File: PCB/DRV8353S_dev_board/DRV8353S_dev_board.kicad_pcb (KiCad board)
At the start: 4 copper layers, 100 x 100 mm, 139 parts, among them J1 HC_POWER, J2 MOT_LC, J3 SWD, J4 EXT_CMD, J5 PHASE, Q1 BSS84, Q2 CSD19502, Q3 CSD19502, Q4 CSD19502, Q5 CSD19502, Q6 CSD19502, Q7 CSD19502, SW1 B3U, SW2 B3U, SW3 B3U, SW4 B3U, SW5 DIP, U1 ECS-33B, U2 STM32F042K4Ux, U3 MIC5283-3.3ML-TR, U4 MIC5283-5.0ML-TR, U5 DRV8353SM

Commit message: more routing work
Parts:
- added C35: 22nF, Capacitor_SMD:C_0603_1608Metric, F.Cu at (86.0, 125.4)
- added R56: 330, Resistor_SMD:R_0603_1608Metric, F.Cu at (86.0, 123.9)
- added REF**: MountingHole_3mm_Pad_Via, MountingHole:MountingHole_3mm_Pad_Via, F.Cu at (145.0, 130.0)
- added REF**: MountingHole_3mm_Pad_Via, MountingHole:MountingHole_3mm_Pad_Via, F.Cu at (55.0, 130.0)
- added TP20: THT, DRV8353S_dev_board:keystone_5001, F.Cu at (62.8, 105.5)
- C14, C15, C16: moved to B.Cu
- moved TP2 211.1 mm to (65.0, 86.1)
- moved TP1 211.0 mm to (64.6, 95.1)
- moved D4 205.6 mm to (56.1, 111.6), turned to 180 degrees
- moved C4 204.9 mm to (57.5, 99.4), turned to 90 degrees
- moved D5 196.8 mm to (61.5, 123.2), turned to 180 degrees
- moved C19 193.4 mm to (79.4, 156.4)
- moved R26 191.3 mm to (79.2, 159.0)
- moved D3 189.0 mm to (63.6, 131.6), turned to 90 degrees
- moved C1 188.4 mm to (77.5, 125.0), turned to 90 degrees
- moved C3 188.3 mm to (58.0, 85.2), turned to 270 degrees
- moved C17 187.9 mm to (86.0, 122.4)
- moved D6 187.4 mm to (65.2, 131.7), turned to 90 degrees
- moved R7 185.4 mm to (61.9, 128.6), turned to 90 degrees
- moved C15 185.2 mm to (72.1, 117.8), turned to 90 degrees
- moved C13 183.3 mm to (65.0, 89.6), turned to 270 degrees
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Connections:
- R10 pad 1: /HALLB_JMP -> /HALLB
- R21 pad 1: /HALLC_JMP -> /HALLC
- R9 pad 1: /HALLA_JMP -> /HALLA
- TP3 pad 1: /HALLA_JMP -> /HALLA
- TP5 pad 1: /HALLB_JMP -> /HALLB
- TP6 pad 1: /HALLC_JMP -> /HALLC
- U2 pad 6: /I_PHASE_A_JMP -> /MOT_TEMP_JMP
- U2 pad 7: /I_PHASE_B_JMP -> /I_PHASE_C_JMP
- U2 pad 8: /I_PHASE_C_JMP -> /I_PHASE_B_JMP
- U2 pad 9: /MOT_TEMP -> /I_PHASE_A_JMP
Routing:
- net GND: track 126.7 -> 2.00 mm, vias 57 -> 1
- net /GATE_HI_C: track 80.7 -> 0.00 mm, vias 2 -> 0
- net /HALLC: track 0.00 -> 79.7 mm, vias 0 -> 1
- net /HALLA: track 0.00 -> 73.4 mm, vias 0 -> 2
- net /HALLB: track 0.00 -> 71.4 mm, vias 0 -> 2
- net /GATE_LO_C: track 61.2 -> 0.00 mm, vias 2 -> 0
- net /DIRECTION_DIP: track 0.00 -> 60.6 mm
- net /MOT_C: track 57.2 -> 0.00 mm, vias 21 -> 0
- net /SHUNT_POS_C: track 56.0 -> 0.00 mm, vias 2 -> 0
- net /~SPEED_UP_PB: track 0.00 -> 52.2 mm
- net /~SPEED_DOWN_PB: track 0.00 -> 47.5 mm
- net /GATE_HI_B: track 43.7 -> 0.00 mm, vias 2 -> 0
- net /~BRAKE_PB: track 0.00 -> 41.1 mm
- net /~RESET_PB: track 0.00 -> 36.2 mm, vias 0 -> 2
- net /GATE_LO_B: track 33.7 -> 0.00 mm, vias 2 -> 0
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- removed copper zone on B.Cu, net (none)
- removed copper zone on B.Cu, net /MOT_A
- removed copper zone on F.Cu, net /MOT_A
- removed copper zone on In1.Cu, net /MOT_A
- removed copper zone on B.Cu, net /MOT_B
- removed copper zone on F.Cu, net /MOT_B
- removed copper zone on In1.Cu, net /MOT_B
- removed copper zone on B.Cu, net /MOT_C
- removed copper zone on F.Cu, net /MOT_C
- removed copper zone on In1.Cu, net /MOT_C
- removed copper zone on F.Cu, net /SHUNT_POS_A
- removed copper zone on F.Cu, net /SHUNT_POS_B
- removed copper zone on F.Cu, net /SHUNT_POS_C
- removed copper zone on B.Cu, net GND
- removed copper zone on F.Cu, net GND
- removed copper zone on In1.Cu, net GND
- removed copper zone on In2.Cu, net GND
- removed copper zone on F.Cu, net Vdrive
- removed copper zone on In1.Cu, net Vdrive
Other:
- board size 100 x 100 mm -> 100 x 85 mm

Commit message: Final (?) layout
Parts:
- removed R36, R37: 0, Resistor_SMD:R_0603_1608Metric
- moved R16 99.9 mm to (65.8, 115.6), turned to 180 degrees
- moved R33 96.1 mm to (78.9, 110.2), turned to 270 degrees
- moved R17 95.2 mm to (65.8, 117.2), turned to 180 degrees
- moved R18 86.2 mm to (71.1, 110.2), turned to 90 degrees
- moved C31 83.3 mm to (95.4, 105.4), turned to 180 degrees
- moved R15 67.5 mm to (76.0, 125.0), turned to 270 degrees
- moved TP20 60.8 mm to (123.0, 97.0)
- moved C23 58.8 mm to (65.8, 112.6), turned to 180 degrees
- moved R32 56.0 mm to (65.8, 114.1)
- moved R34 50.6 mm to (74.5, 126.8), turned to 90 degrees
- moved R27 49.7 mm to (69.6, 110.2), turned to 90 degrees
- moved R26 49.0 mm to (74.3, 110.3), turned to 270 degrees
- moved C21 48.8 mm to (68.1, 110.2), turned to 90 degrees
- moved C22 46.9 mm to (65.8, 120.2)
- moved C19 46.6 mm to (72.7, 110.2), turned to 90 degrees
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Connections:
- J3 pad 2: Net-(D4-Pad2) -> GND
- J3 pad 4: /~RESET_PB -> Net-(J3-Pad4)
- J3 pad 5: Net-(J3-Pad5) -> Net-(D4-Pad2)
- J3 pad 6: GND -> /~RESET_PB
- TP20 pad 1: /MOT_TEMP_JMP -> /MOT_TEMP
- U2 pad 14: /SPEED_PWM_JMP -> /~DRV8353_FAULT_JMP
- U2 pad 15: /DIRECTION_JMP -> /DRV8353_EN_JMP
- U2 pad 16: /~BRAKE_JMP -> /DIRECTION_JMP
- U2 pad 18: /DRV8353_EN_JMP -> /~BRAKE_JMP
- U2 pad 21: /DIRECTION_DIP -> /~SYS_FAULT
- U2 pad 22: /~SPEED_UP_PB -> /~LED_SPEED
- U2 pad 25: Net-(U2-Pad25) -> /~LED_DIR
- U2 pad 26: /~DRV8353_FAULT_JMP -> /~BRAKE_PB
- U2 pad 27: /~LED_DIR -> /~SPEED_DOWN_PB
- U2 pad 28: /~LED_SPEED -> /~SPEED_UP_PB
- U2 pad 29: /~SYS_FAULT -> /DIRECTION_DIP
- U2 pad 30: /~SPEED_DOWN_PB -> Net-(U2-Pad30)
- U2 pad 32: /~BRAKE_PB -> /SPEED_PWM_JMP
- U2 pad 6: /MOT_TEMP_JMP -> /I_PHASE_C_JMP
- U2 pad 7: /I_PHASE_C_JMP -> /I_PHASE_B_JMP
- U2 pad 8: /I_PHASE_B_JMP -> /I_PHASE_A_JMP
- U2 pad 9: /I_PHASE_A_JMP -> /MOT_TEMP_JMP
- U5 pad 41: (no net) -> GND
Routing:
- net /HALLC: track 79.7 -> 0.00 mm, vias 1 -> 0
- net /HALLA: track 73.4 -> 0.00 mm, vias 2 -> 0
- net /HALLB: track 71.4 -> 0.00 mm, vias 2 -> 0
- net /DIRECTION_DIP: track 60.6 -> 0.00 mm
- net /~SPEED_UP_PB: track 52.2 -> 0.00 mm
- net /~SPEED_DOWN_PB: track 47.5 -> 0.00 mm
- net /~BRAKE_PB: track 41.1 -> 0.00 mm
- net /~RESET_PB: track 36.2 -> 0.00 mm, vias 2 -> 0
- net /~DRV8353_FAULT: track 19.7 -> 0.00 mm
- net /I_PHASE_C: track 19.3 -> 0.00 mm
- net /EXT_UART_RX: track 18.9 -> 0.00 mm, vias 2 -> 0
- net /I_PHASE_B: track 18.7 -> 0.00 mm
- net /I_PHASE_A: track 18.2 -> 0.00 mm
- net /EXT_UART_TX: track 17.8 -> 0.00 mm
- net /MOT_TEMP_JMP: track 14.3 -> 0.00 mm
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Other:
- outline, holes or cut-outs redrawn
- board text added: "High Current Stack up: Top: Vdrive Mid1: Vdrive Mid2: DRV Sig and GND Bottom: GND"
- board text added: "Low Current Stack up: Top: Signal Mid1: GND Mid2: Power Bottom: Signal + GND"

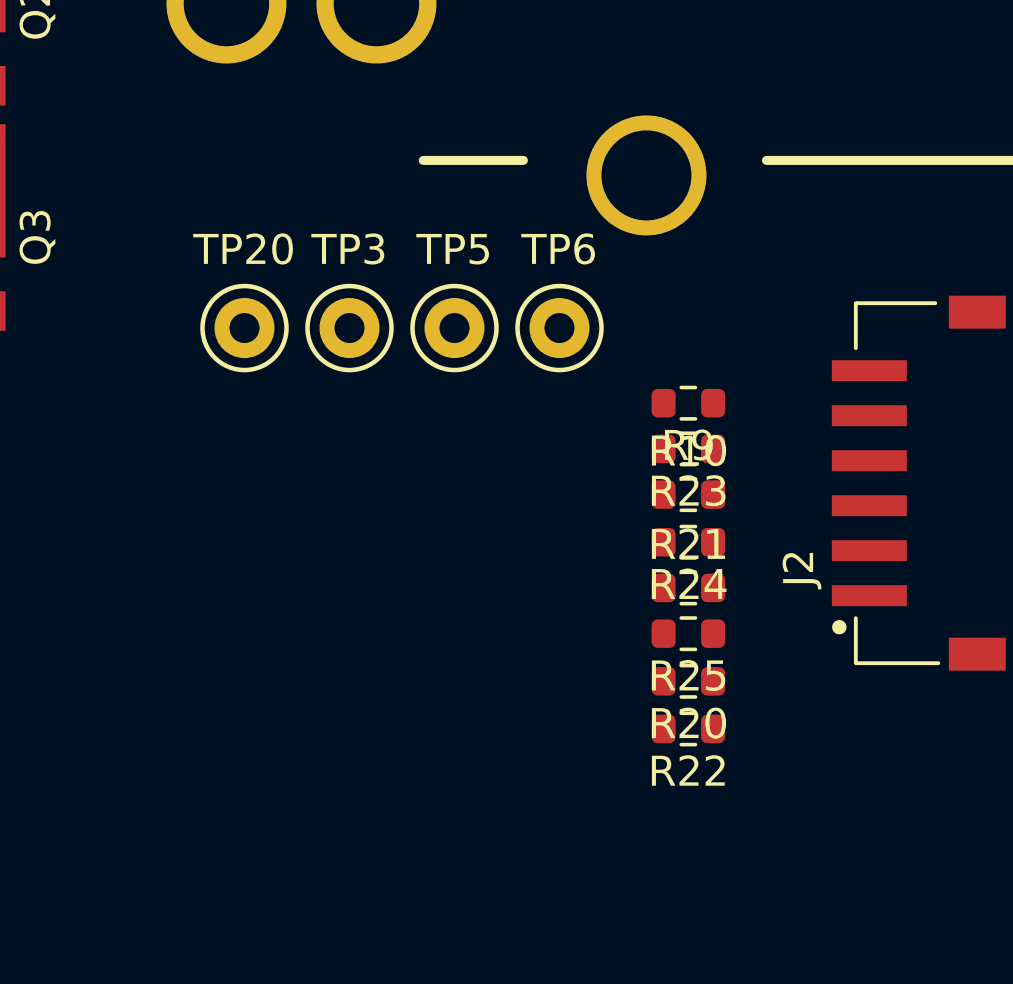
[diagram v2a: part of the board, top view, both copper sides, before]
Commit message: Final Routing
Moved around encoder stuff. Also added decoupling capacitor near encoder connector.
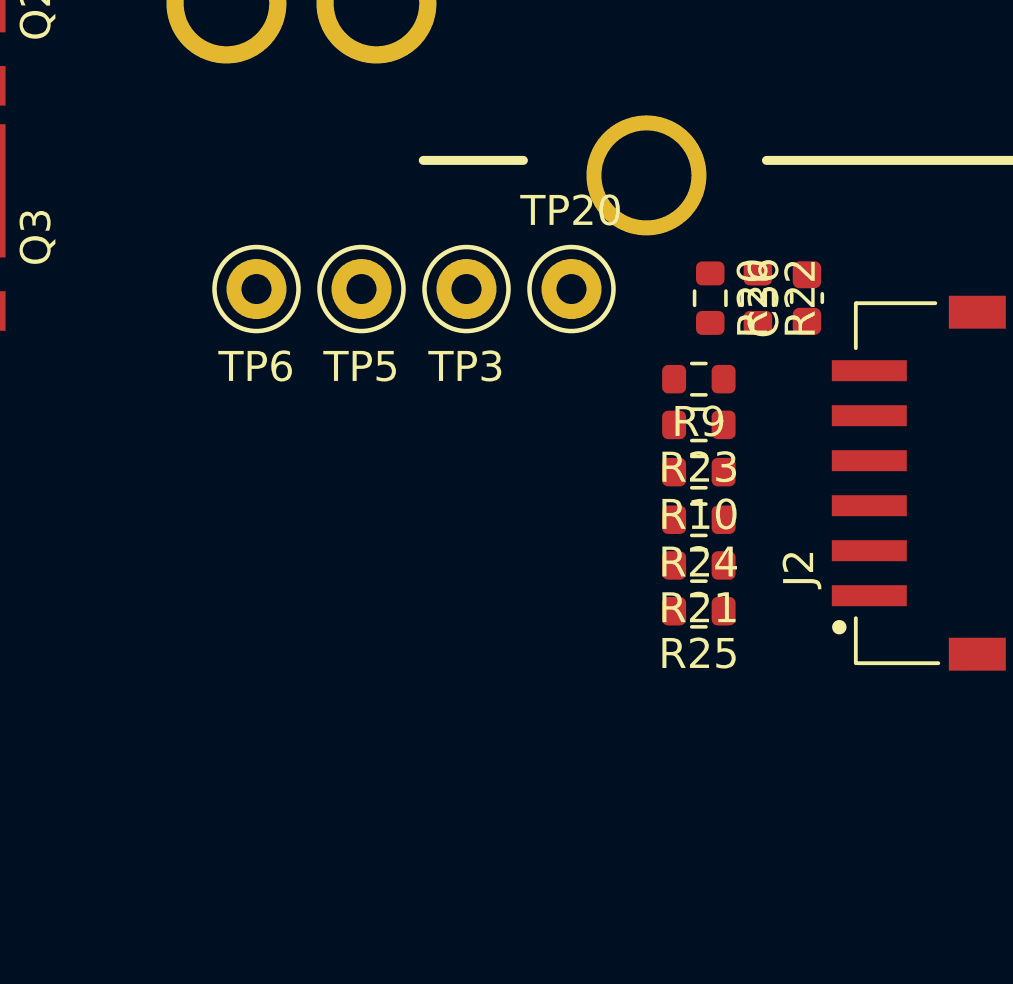
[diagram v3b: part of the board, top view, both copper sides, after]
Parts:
- added C36: 22nF, Capacitor_SMD:C_0603_1608Metric, F.Cu at (141.8, 96.0)
- moved R22 14.5 mm to (140.1, 96.0), turned to 270 degrees
- moved R20 12.8 mm to (138.5, 96.0), turned to 270 degrees
- moved TP20 11.0 mm to (133.9, 95.7)
- moved TP6 10.2 mm to (123.4, 95.7), turned to 180 degrees
- moved TP3 4.11 mm to (130.4, 95.7), turned to 180 degrees
- moved TP5 3.36 mm to (126.9, 95.7), turned to 180 degrees
- moved R9 0.87 mm to (138.1, 98.7)
- moved R23 0.87 mm to (138.1, 100.2)
- moved R10 0.83 mm to (138.1, 101.8), turned to 180 degrees
- moved R21 0.83 mm to (138.1, 104.9), turned to 180 degrees
- moved R25 0.83 mm to (138.1, 106.4)
- moved R24 0.83 mm to (138.1, 103.4)
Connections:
- R10 pad 1: /HALLB -> /HALLB_JMP
- R21 pad 1: /HALLC -> /HALLC_JMP
- R9 pad 1: /HALLA -> /HALLA_JMP

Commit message: High Current Routing
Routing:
- net Vdrive: vias 0 -> 91
- net GND: vias 0 -> 146
- net /MOT_C: vias 0 -> 48
- net /MOT_B: vias 0 -> 49
- net /MOT_A: vias 0 -> 50
- added copper zone on B.Cu, net /MOT_A
- added copper zone on F.Cu, net /MOT_A
- added copper zone on In1.Cu, net /MOT_A
- added copper zone on In2.Cu, net /MOT_A
- added copper zone on B.Cu, net /MOT_B
- added copper zone on F.Cu, net /MOT_B
- added copper zone on In1.Cu, net /MOT_B
- added copper zone on In2.Cu, net /MOT_B
- added copper zone on B.Cu, net /MOT_C
- added copper zone on F.Cu, net /MOT_C
- added copper zone on In1.Cu, net /MOT_C
- added copper zone on In2.Cu, net /MOT_C
- added copper zone on F.Cu, net /SHUNT_POS_A
- added copper zone on F.Cu, net /SHUNT_POS_B
- added copper zone on F.Cu, net /SHUNT_POS_C
- added copper zone on B.Cu, net GND
- added copper zone on F.Cu, net GND
- added copper zone on In1.Cu, net GND
- added copper zone on In2.Cu, net GND
- added copper zone on F.Cu, net Vdrive
- added copper zone on In1.Cu, net Vdrive

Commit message: Most DRV routing done.
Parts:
- moved TP10 6.99 mm to (67.5, 104.7)
- moved TP12 6.99 mm to (71.0, 104.7)
- moved TP8 6.99 mm to (74.5, 104.7)
- moved TP9 6.99 mm to (64.0, 104.7)
- moved C22 2.90 mm to (68.5, 121.3)
- moved C23 2.90 mm to (68.5, 113.7)
- moved R16 2.90 mm to (68.5, 116.8)
- moved R17 2.90 mm to (68.5, 118.3)
- moved R28 2.90 mm to (68.5, 119.8)
- moved R32 2.90 mm to (68.5, 115.3)
- moved C17 1.14 mm to (85.7, 124.7)
- moved C18 1.14 mm to (85.7, 121.6)
- moved C20 1.14 mm to (85.7, 118.5)
- moved C35 1.14 mm to (85.7, 115.4)
- moved R29 1.14 mm to (85.7, 117.0)
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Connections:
- REF** pad 1: (no net) -> GND (x4)
- TP11 pad 1: /I_PHASE_A_JMP -> /I_PHASE_A
- TP4 pad 1: /I_PHASE_C_JMP -> /I_PHASE_C
- TP7 pad 1: /I_PHASE_B_JMP -> /I_PHASE_B
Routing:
- net GND: track 0.00 -> 134.6 mm, vias 146 -> 155
- net /GATE_HI_C: track 0.42 -> 78.6 mm, vias 0 -> 2
- net /HALLC: track 0.00 -> 77.4 mm, vias 0 -> 2
- net /MOT_TEMP: track 0.00 -> 76.1 mm, vias 0 -> 2
- net /HALLB: track 0.00 -> 75.2 mm, vias 0 -> 2
- net /HALLA: track 0.00 -> 72.3 mm
- net /MOT_C: track 0.00 -> 60.1 mm, vias 48 -> 49
- net /GATE_LO_C: track 0.00 -> 58.9 mm, vias 0 -> 2
- net /SHUNT_POS_C: track 0.00 -> 51.0 mm, vias 0 -> 2
- net /I_PHASE_C: track 0.00 -> 48.3 mm, vias 0 -> 2
- net /GATE_HI_B: track 0.00 -> 46.6 mm, vias 0 -> 2
- net /GATE_LO_B: track 0.00 -> 45.5 mm, vias 0 -> 2
- net /I_PHASE_B: track 0.00 -> 40.8 mm, vias 0 -> 2
- net /GATE_HI_A: track 0.00 -> 36.3 mm, vias 0 -> 2
- net /MOT_B: track 0.00 -> 35.9 mm, vias 49 -> 50
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
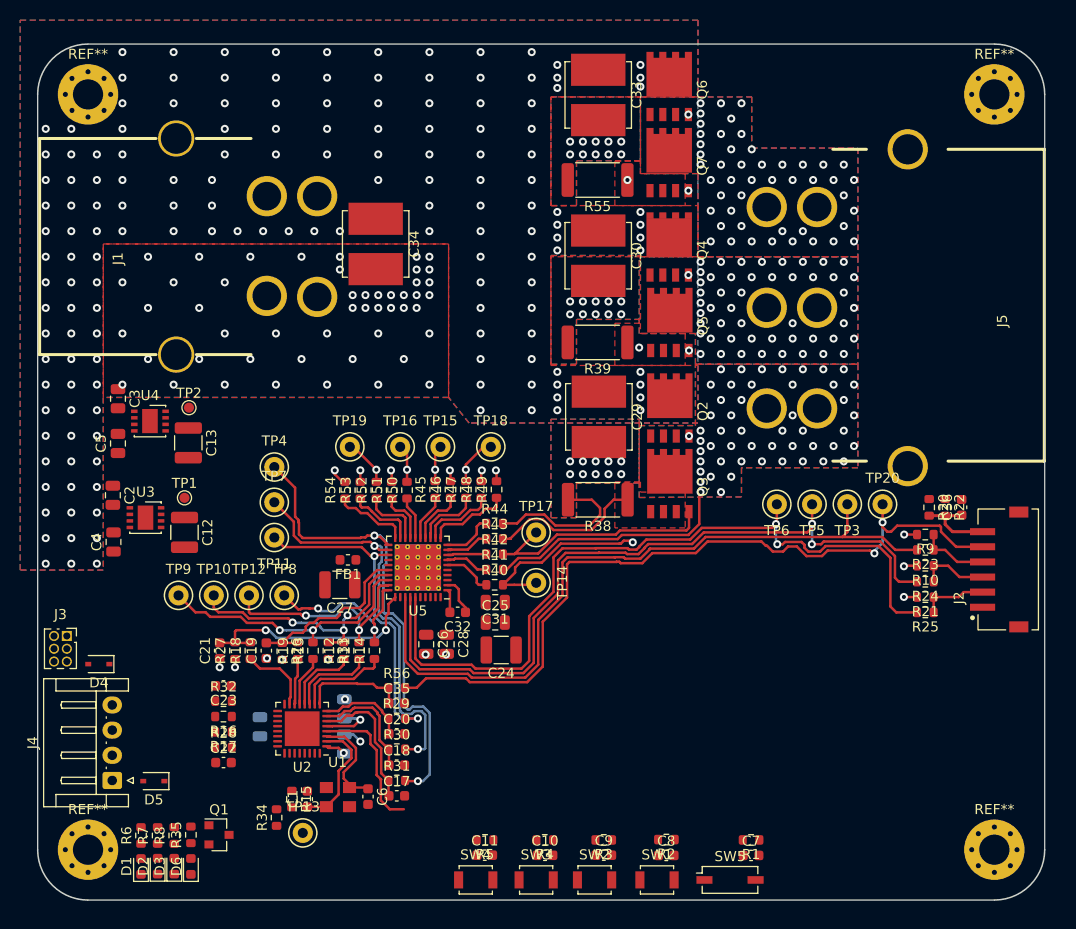
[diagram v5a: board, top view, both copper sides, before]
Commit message: Finished routing (?)
All signals routed. No DRC errors.
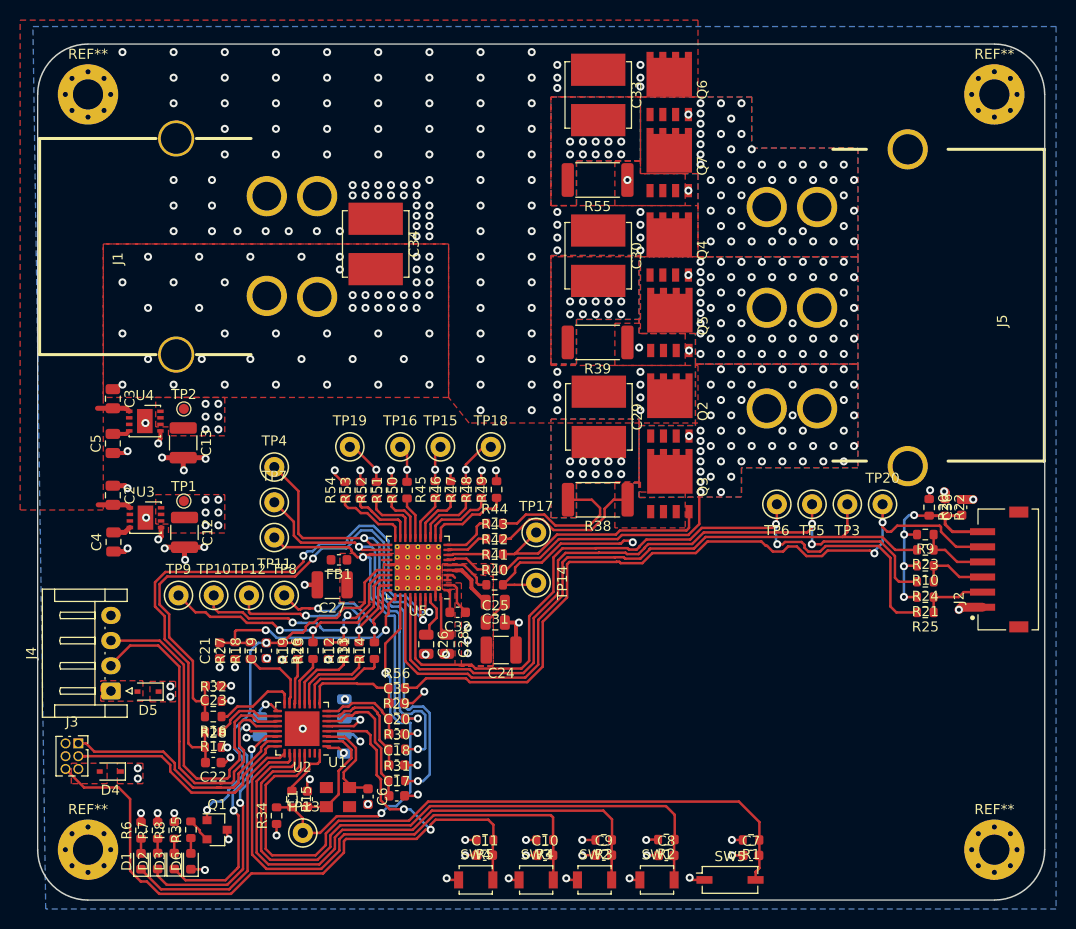
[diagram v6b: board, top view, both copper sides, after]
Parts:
- moved J3 10.7 mm to (54.0, 119.4)
- moved D4 10.7 mm to (57.2, 122.2)
- moved D5 8.91 mm to (61.0, 114.3)
- moved J4 8.89 mm to (57.3, 114.2)
- moved C22 1.02 mm to (67.4, 121.3), turned to 180 degrees
- moved C23 1.02 mm to (67.4, 113.7)
- moved R16 1.02 mm to (67.4, 116.8)
- moved R17 1.02 mm to (67.4, 118.3)
- moved R28 1.02 mm to (67.4, 119.8)
- moved R32 1.02 mm to (67.4, 115.3)
- moved FB1 0.89 mm to (79.9, 101.2)
- moved C27 0.76 mm to (79.2, 103.7)
- moved Q1 0.54 mm to (67.8, 128.0)
- moved TP2 0.52 mm to (64.5, 86.2)
- moved D1 0.51 mm to (60.3, 131.2)
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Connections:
- J4 pad 2: /EXT_UART_TX -> /EXT_UART_RX
- J4 pad 3: /EXT_UART_RX -> /EXT_UART_TX
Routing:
- net +5V: track 0.00 -> 206.3 mm, vias 0 -> 7
- net /DIRECTION_DIP: track 0.00 -> 71.3 mm
- net /~RESET_PB: track 14.1 -> 79.1 mm, vias 0 -> 2
- net /~SPEED_UP_PB: track 0.00 -> 63.7 mm
- net /~BRAKE: track 0.00 -> 60.6 mm, vias 0 -> 2
- net GND: track 134.6 -> 194.8 mm, vias 155 -> 162
- net /~SPEED_DOWN_PB: track 0.00 -> 57.7 mm
- net /DIRECTION: track 0.00 -> 54.6 mm, vias 0 -> 2
- net /~BRAKE_PB: track 0.00 -> 52.4 mm
- net Vdrive: track 0.00 -> 39.6 mm, vias 89 -> 81
- net /SPEED_PWM: track 0.00 -> 38.6 mm, vias 0 -> 2
- net /EXT_UART_RX: track 0.00 -> 35.4 mm
- net /EXT_UART_TX: track 0.00 -> 34.2 mm
- net +3V3: track 7.46 -> 38.0 mm, vias 4 -> 27
- net /~LED_SPEED: track 0.00 -> 26.3 mm, vias 0 -> 2
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- added copper zone on F.Cu, net +3V3
- added copper zone on In2.Cu, net +3V3
- added copper zone on F.Cu, net +5V
- added copper zone on F.Cu, net Net-(C27-Pad1)
- added copper zone on F.Cu, net Net-(D4-Pad2)
- added copper zone on F.Cu, net Net-(D5-Pad2)
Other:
- net class 35 added: clearance 0.2, trace_width 0.25, via_dia 0.8, via_drill 0.4
- rule via_min_size: 0.4 -> 0.399796

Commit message: final final routing
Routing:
- net GND: vias 162 -> 177
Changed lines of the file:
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@@
     (thickness 1.6)
     (drawings 12)
-    (tracks 1850)
+    (tracks 1865)
     (zones 0)
     (modules 143)
@@
   (via (at 77.724 68.58) (size 0.8) (drill 0.4) (layers F.Cu B.Cu) (net 2))
   (via (at 72.644 68.58) (size 0.8) (drill 0.4) (layers F.Cu B.Cu) (net 2))
+  (via (at 114.3 111.76) (size 0.8) (drill 0.4) (layers F.Cu B.Cu) (net 2))
+  (via (at 124.46 116.84) (size 0.8) (drill 0.4) (layers F.Cu B.Cu) (net 2))
+  (via (at 134.62 111.76) (size 0.8) (drill 0.4) (layers F.Cu B.Cu) (net 2))
+  (via (at 124.46 104.14) (size 0.8) (drill 0.4) (layers F.Cu B.Cu) (net 2))
+  (via (at 139.7 83.82) (size 0.8) (drill 0.4) (layers F.Cu B.Cu) (net 2))
+  (via (at 137.16 73.66) (size 0.8) (drill 0.4) (layers F.Cu B.Cu) (net 2))
+  (via (at 147.32 68.58) (size 0.8) (drill 0.4) (layers F.Cu B.Cu) (net 2))
+  (via (at 132.08 55.88) (size 0.8) (drill 0.4) (layers F.Cu B.Cu) (net 2))
+  (via (at 137.16 53.34) (size 0.8) (drill 0.4) (layers F.Cu B.Cu) (net 2))
+  (via (at 121.92 53.34) (size 0.8) (drill 0.4) (layers F.Cu B.Cu) (net 2))
+  (via (at 147.32 91.44) (size 0.8) (drill 0.4) (layers F.Cu B.Cu) (net 2))
+  (via (at 134.62 132.08) (size 0.8) (drill 0.4) (layers F.Cu B.Cu) (net 2))
+  (via (at 144.78 121.92) (size 0.8) (drill 0.4) (layers F.Cu B.Cu) (net 2))
+  (via (at 129.54 129.54) (size 0.8) (drill 0.4) (layers F.Cu B.Cu) (net 2))
+  (via (at 53.34 109.22) (size 0.8) (drill 0.4) (layers F.Cu B.Cu) (net 2))
   (via (at 68.58 50.8) (size 0.8) (drill 0.4) (layers F.Cu B.Cu) (net 3))
   (via (at 78.74 50.8) (size 0.8) (drill 0.4) (layers F.Cu B.Cu) (net 3))
@@
   (segment (start 136.0425 98.7045) (end 136.0425 101.8285) (width 0.25) (layer B.Cu) (net 99))
   (segment (start 136.017 101.854) (end 136.017 104.902) (width 0.25) (layer B.Cu) (net 99))
-  (zone (net 2) (net_name GND) (layer F.Cu) (hatch edge 0.508)
-    (priority 100)
-    (connect_pads (clearance 0.3))
-    (min_thickness 0.254)
-    (fill yes (arc_segments 32) (thermal_gap 0.3) (thermal_bridge_width 2) (smoothing fillet) (radius 1))
-    (polygon
-      (pts
-        (xy 90.805 85.09) (xy 56.515 85.09) (xy 56.515 69.85) (xy 90.805 69.85)
-      )
-    )
-  )
   (zone (net 57) (net_name /SHUNT_POS_C) (layer F.Cu) (hatch edge 0.508)
     (priority 100)
@@
       )
     )
+  )
+  (zone (net 2) (net_name GND) (layer F.Cu) (hatch edge 0.508)
+    (connect_pads yes (clearance 0.3))
+    (min_thickness 0.254)
+    (fill yes (arc_segments 32) (thermal_gap 0.3) (thermal_bridge_width 2) (smoothing fillet) (radius 0.5))
+    (polygon
+      (pts
+        (xy 154.94 137.16) (xy 48.26 137.16) (xy 48.26 48.26) (xy 154.94 48.26)
+      )
+    )
